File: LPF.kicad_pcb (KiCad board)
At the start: 4 copper layers, 100 x 100 mm, 139 parts, among them J1 Conn_02x05_Counter_Clockwise, P1 SMA, P3 SMA, P4 SMA

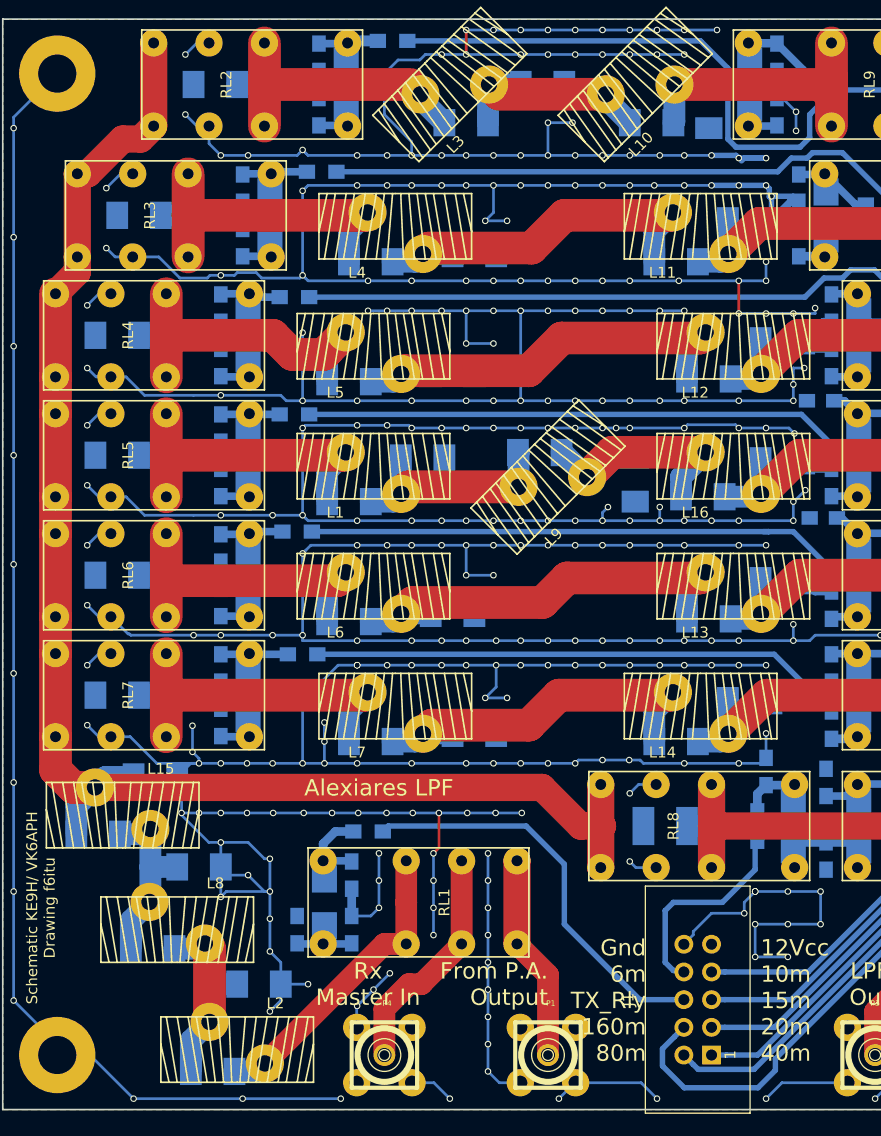
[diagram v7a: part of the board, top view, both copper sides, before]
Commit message: Caps changed for ATC-B footprint. Under dev., unstable
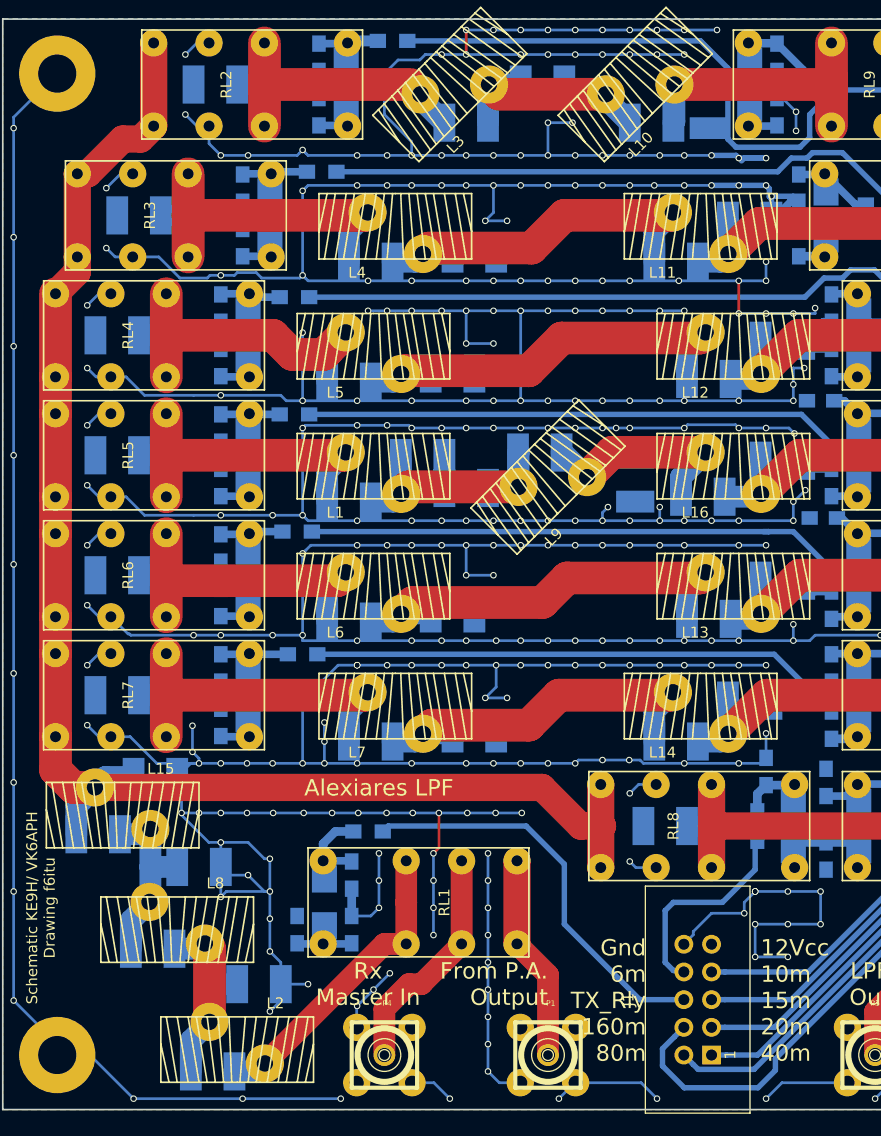
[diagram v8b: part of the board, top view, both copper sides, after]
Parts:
- C11, C16, C17, C18, C19, C20, C21, C22, C23, C24, C25, C26, C27, C28, C29, C30, C31, C32, C33, C34, C35, C36, C37, C38, C39, C40, C41, C42, C43, C44, C45, C46, C47, C48, C49, C50, C51, C55, C59: footprint Capacitors_SMD:C_1210_HandSoldering -> ATC_B:ATC_500_HandSoldering
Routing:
- net 160m: track 181.3 -> 166.6 mm
- net GND: track 1293.6 -> 1308.3 mm
